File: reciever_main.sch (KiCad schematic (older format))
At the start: 1 part, among them J1 QUARTET_RECV

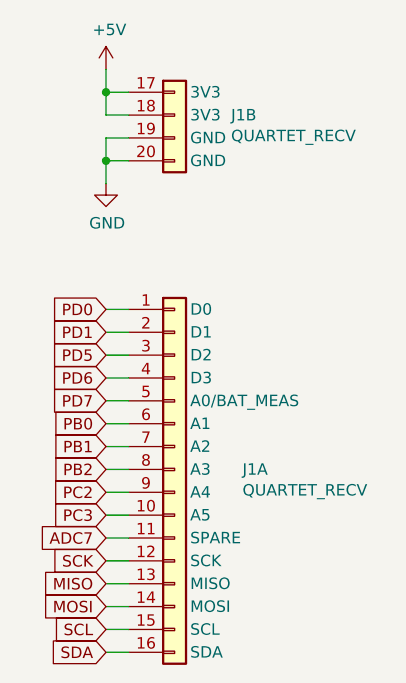
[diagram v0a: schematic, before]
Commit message: Layout and route numpad matrix
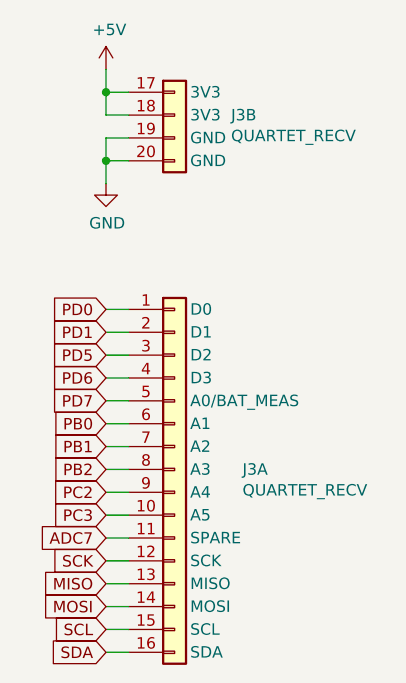
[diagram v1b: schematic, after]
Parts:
- renumbered J1 to J3
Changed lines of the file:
@@
 $Descr A4 11693 8268
 encoding utf-8
-Sheet 2 3
+Sheet 3 3
 Title ""
 Date ""
@@
 P 1350 1100
 AR Path="/5FF53271/5FF77D09" Ref="#PWR?"  Part="1"
-AR Path="/5FF53271/5FF7CBCC/5FF77D09" Ref="#PWR?"  Part="1"
-AR Path="/5FF77C4F/5FF77D09" Ref="#PWR01"  Part="1"
-F 0 "#PWR01" H 1350 950 50  0001 C CNN
+AR Path="/5FF53271/5FF7CBCC/5FF77D09" Ref="#PWR016"  Part="1"
+AR Path="/5FF77C4F/5FF77D09" Ref="#PWR?"  Part="1"
+F 0 "#PWR016" H 1350 950 50  0001 C CNN
 F 1 "+5V" H 1365 1273 50  0000 C CNN
 F 2 "" H 1350 1100 50  0001 C CNN
@@
 P 1350 1600
 AR Path="/5FF53271/5FF77D0A" Ref="#PWR?"  Part="1"
-AR Path="/5FF53271/5FF7CBCC/5FF77D0A" Ref="#PWR?"  Part="1"
-AR Path="/5FF77C4F/5FF77D0A" Ref="#PWR02"  Part="1"
-F 0 "#PWR02" H 1350 1350 50  0001 C CNN
+AR Path="/5FF53271/5FF7CBCC/5FF77D0A" Ref="#PWR017"  Part="1"
+AR Path="/5FF77C4F/5FF77D0A" Ref="#PWR?"  Part="1"
+F 0 "#PWR017" H 1350 1350 50  0001 C CNN
 F 1 "GND" H 1355 1427 50  0000 C CNN
 F 2 "" H 1350 1600 50  0001 C CNN
@@
 	1350 3650 1450 3650
 $Comp
-L gigahawk:QUARTET_RECV J1
+L gigahawk:QUARTET_RECV J3
 U 1 1 5FF794DA
 P 1650 2100
-F 0 "J1" H 1947 1350 50  0000 L CNN
+F 0 "J3" H 1947 1350 50  0000 L CNN
 F 1 "QUARTET_RECV" H 1947 1259 50  0000 L CNN
 F 2 "Gigahawk:QUARTET_RECV_MAIN" H 1700 2100 50  0001 C CNN
@@
 $EndComp
 $Comp
-L gigahawk:QUARTET_RECV J1
+L gigahawk:QUARTET_RECV J3
 U 2 1 5FF7AE7A
 P 1650 1150
-F 0 "J1" H 1897 1000 50  0000 L CNN
+F 0 "J3" H 1897 1000 50  0000 L CNN
 F 1 "QUARTET_RECV" H 1897 909 50  0000 L CNN
 F 2 "Gigahawk:QUARTET_RECV_MAIN" H 1700 1150 50  0001 C CNN

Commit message: Reroute matrix, redo schematics for feather compat
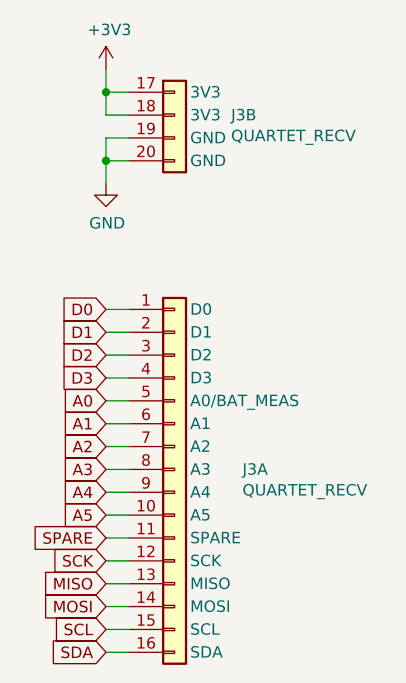
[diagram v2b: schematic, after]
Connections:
- net +5V renamed +3V3
- net ADC7 renamed SPARE
- net PB0 renamed A1
- net PB1 renamed A2
- net PB2 renamed A3
- net PC2 renamed A4
- net PC3 renamed A5
- net PD0 renamed D0
- net PD1 renamed D1
- net PD5 renamed D2
- net PD6 renamed D3
- net PD7 renamed A0
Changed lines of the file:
@@
 $Descr A4 11693 8268
 encoding utf-8
-Sheet 3 3
+Sheet 2 3
 Title ""
 Date ""
@@
 $EndDescr
 $Comp
-L power:+5V #PWR?
-U 1 1 5FF77D09
-P 1350 1100
-AR Path="/5FF53271/5FF77D09" Ref="#PWR?"  Part="1"
-AR Path="/5FF53271/5FF7CBCC/5FF77D09" Ref="#PWR016"  Part="1"
-AR Path="/5FF77C4F/5FF77D09" Ref="#PWR?"  Part="1"
-F 0 "#PWR016" H 1350 950 50  0001 C CNN
-F 1 "+5V" H 1365 1273 50  0000 C CNN
-F 2 "" H 1350 1100 50  0001 C CNN
-F 3 "" H 1350 1100 50  0001 C CNN
-	1    1350 1100
-	1    0    0    -1
-$EndComp
-$Comp
 L power:GND #PWR?
 U 1 1 5FF77D0A
@@
 AR Path="/5FF53271/5FF7CBCC/5FF77D0A" Ref="#PWR017"  Part="1"
 AR Path="/5FF77C4F/5FF77D0A" Ref="#PWR?"  Part="1"
-F 0 "#PWR017" H 1350 1350 50  0001 C CNN
+F 0 "#PWR?" H 1350 1350 50  0001 C CNN
 F 1 "GND" H 1355 1427 50  0000 C CNN
 F 2 "" H 1350 1600 50  0001 C CNN
@@
 Connection ~ 1350 1500
 Text GLabel 1350 2250 0    50   Input ~ 0
-PD1
+D1
 Text GLabel 1350 2150 0    50   Input ~ 0
-PD0
+D0
 Text GLabel 1350 2350 0    50   Input ~ 0
-PD5
+D2
 Text GLabel 1350 2450 0    50   Input ~ 0
-PD6
+D3
 Text GLabel 1350 2550 0    50   Input ~ 0
-PD7
+A0
 Text GLabel 1350 2650 0    50   Input ~ 0
-PB0
+A1
 Text GLabel 1350 2750 0    50   Input ~ 0
-PB1
+A2
 Text GLabel 1350 2850 0    50   Input ~ 0
-PB2
+A3
 Text GLabel 1350 2950 0    50   Input ~ 0
-PC2
+A4
 Text GLabel 1350 3050 0    50   Input ~ 0
-PC3
+A5
 Text GLabel 1350 3150 0    50   Input ~ 0
-ADC7
+SPARE
 Wire Wire Line
 	1350 3150 1450 3150
@@
 U 1 1 5FF794DA
 P 1650 2100
+AR Path="/5FF794DA" Ref="J3"  Part="1"
+AR Path="/5FF77C4F/5FF794DA" Ref="J3"  Part="1"
 F 0 "J3" H 1947 1350 50  0000 L CNN
 F 1 "QUARTET_RECV" H 1947 1259 50  0000 L CNN
@@
 U 2 1 5FF7AE7A
 P 1650 1150
+AR Path="/5FF7AE7A" Ref="J3"  Part="2"
+AR Path="/5FF77C4F/5FF7AE7A" Ref="J3"  Part="2"
 F 0 "J3" H 1897 1000 50  0000 L CNN
 F 1 "QUARTET_RECV" H 1897 909 50  0000 L CNN
@@
 	1    0    0    -1
 $EndComp
+$Comp
+L power:+3V3 #PWR?
+U 1 1 60473FED
+P 1350 1100
+F 0 "#PWR?" H 1350 950 50  0001 C CNN
+F 1 "+3V3" H 1365 1273 50  0000 C CNN
+F 2 "" H 1350 1100 50  0001 C CNN
+F 3 "" H 1350 1100 50  0001 C CNN
+	1    1350 1100
+	1    0    0    -1
+$EndComp

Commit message: Get ready for JLCPCB
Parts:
- J3: Part Numbers (none) -> F519-1A7A1-11004-E200; F519-1A7A1-11016-E200
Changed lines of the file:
@@
 $Descr A4 11693 8268
 encoding utf-8
-Sheet 3 4
+Sheet 2 3
 Title ""
 Date ""
@@
 AR Path="/5FF53271/5FF7CBCC/5FF77D0A" Ref="#PWR017"  Part="1"
 AR Path="/5FF77C4F/5FF77D0A" Ref="#PWR?"  Part="1"
-F 0 "#PWR017" H 1350 1350 50  0001 C CNN
+F 0 "#PWR?" H 1350 1350 50  0001 C CNN
 F 1 "GND" H 1355 1427 50  0000 C CNN
 F 2 "" H 1350 1600 50  0001 C CNN
@@
 F 2 "Gigahawk:QUARTET_RECV_MAIN" H 1700 2100 50  0001 C CNN
 F 3 "" H 1700 2100 50  0001 C CNN
+F 4 "F519-1A7A1-11004-E200; F519-1A7A1-11016-E200" H 1650 2100 50  0001 C CNN "Part Numbers"
 	1    1650 2100
 	1    0    0    -1
